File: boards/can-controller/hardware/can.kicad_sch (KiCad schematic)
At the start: 40 parts, among them J10 CAN1, J11 CAN2, J12 CAN3, J13 CAN4, U10 ISO1044BD, U11 ISO1044BD, U12 ISO1044BD, U13 ISO1044BD

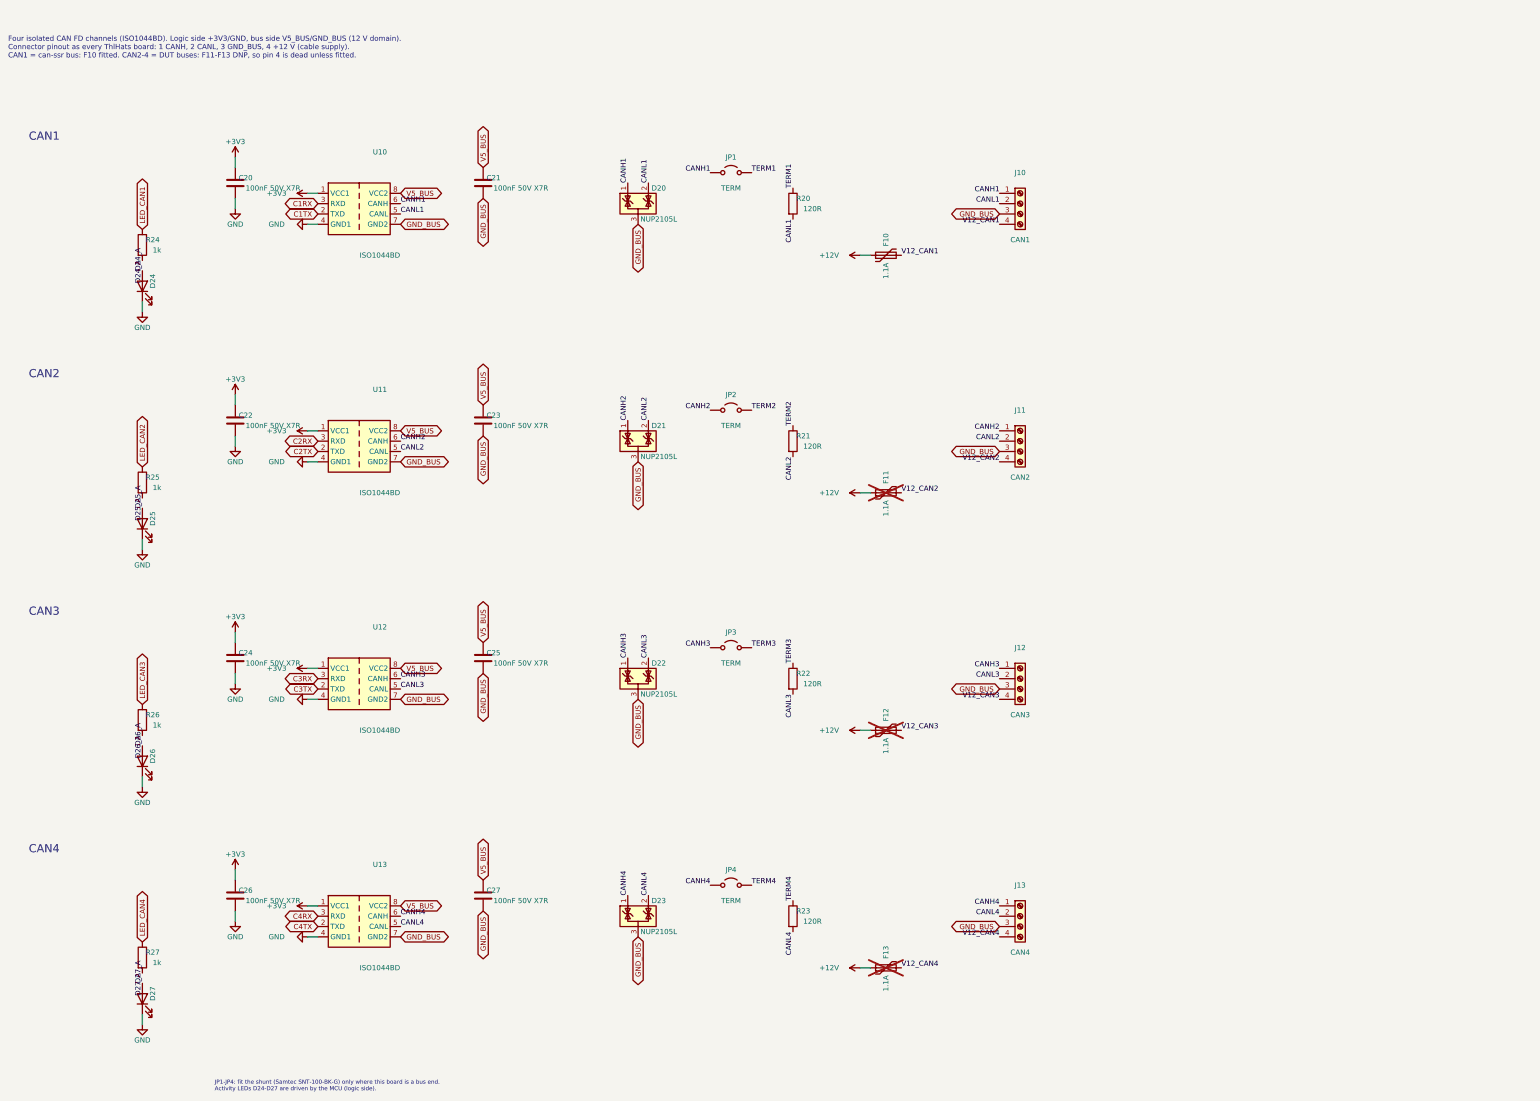
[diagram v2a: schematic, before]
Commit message: can-controller: schematic for the new scope (Ethernet W6100, 4 x ISOW1044, AQW212 relays, diff AI)
Six sheets generated by gen_schematic.py: MCU and logic power, Ethernet,
CAN x4, 12 V input and isolated logic supply (TDN 5-2411WI), relay drive,
GPIO and analog in. ERC 0; netlist check: no net crosses a domain except
at the designed crossings. New lib parts: Thl_Interface:W6100-L (flat),
Thl_Isolator:AQW212, stock ISOW1044 / TDN 5WI / LQFP-48 / bead footprints.
PCB still holds the old layout (next: update from schematic, placement).

Co-Authored-By: Claude Opus 5.5 <noreply@anthropic.com>
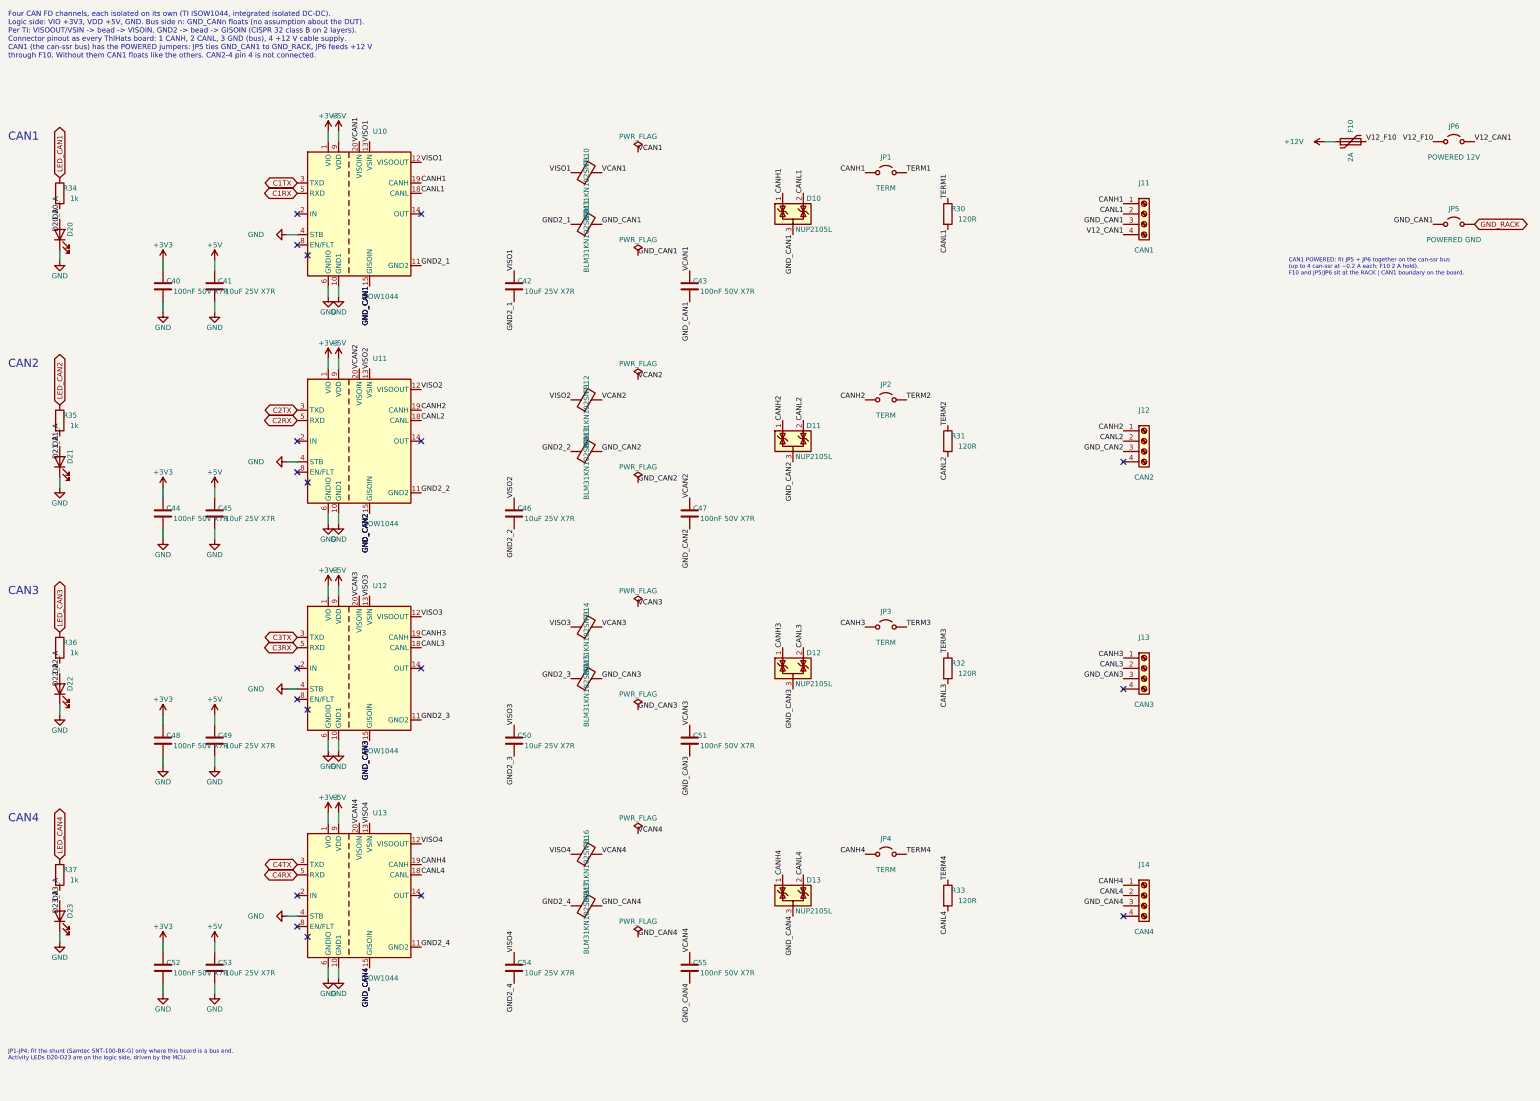
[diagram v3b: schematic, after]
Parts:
- removed C20, C21, C22, C23, C24, C25, C26, C27: 100nF 50V X7R, Capacitor_SMD:C_0805_2012Metric_Pad1.18x1.45mm_HandSolder, symbol Device:C
- removed D20, D21, D22, D23: NUP2105L, Package_TO_SOT_SMD:SOT-23, symbol Power_Protection:NUP2105L
- removed D24, D25, D26, D27: LED yellow, LED_SMD:LED_1206_3216Metric_Pad1.42x1.75mm_HandSolder, symbol Device:LED
- removed F11, F12, F13: 1.1A, Fuse:Fuse_1812_4532Metric_Pad1.30x3.40mm_HandSolder, symbol Device:Polyfuse
- removed J10: CAN1, Connector_Phoenix_MC:PhoenixContact_MC_1,5_4-G-3.5_1x04_P3.50mm_Horizontal, symbol Connector:Screw_Terminal_01x04
- removed R20, R21, R22, R23: 120R, Resistor_SMD:R_1206_3216Metric_Pad1.30x1.75mm_HandSolder, symbol Device:R
- removed R24, R25, R26, R27: 1k, Resistor_SMD:R_1206_3216Metric_Pad1.30x1.75mm_HandSolder, symbol Device:R
- removed U10, U11, U12, U13: ISO1044BD, Package_SO:SOIC-8_3.9x4.9mm_P1.27mm, symbol Interface_CAN_LIN:ISO1044BD
- added C40, C43, C44, C47, C48, C51, C52, C55: 100nF 50V X7R, Capacitor_SMD:C_0805_2012Metric_Pad1.18x1.45mm_HandSolder, symbol Device:C
- added C41, C42, C45, C46, C49, C50, C53, C54: 10uF 25V X7R, Capacitor_SMD:C_1206_3216Metric_Pad1.33x1.80mm_HandSolder, symbol Device:C
- added D10, D11, D12, D13: NUP2105L, Package_TO_SOT_SMD:SOT-23, symbol Power_Protection:NUP2105L
- added D20, D21, D22, D23: LED yellow, LED_SMD:LED_1206_3216Metric_Pad1.42x1.75mm_HandSolder, symbol Device:LED
- added FB10, FB11, FB12, FB13, FB14, FB15, FB16, FB17: BLM31KN102SN1L, Inductor_SMD:L_1206_3216Metric_Pad1.22x1.90mm_HandSolder, symbol Device:FerriteBead
- added J14: CAN4, Connector_Phoenix_MC:PhoenixContact_MC_1,5_4-G-3.5_1x04_P3.50mm_Horizontal, symbol Connector:Screw_Terminal_01x04
- added JP5: POWERED GND, Connector_PinHeader_2.54mm:PinHeader_1x02_P2.54mm_Vertical, symbol Jumper:Jumper_2_Open
- added JP6: POWERED 12V, Connector_PinHeader_2.54mm:PinHeader_1x02_P2.54mm_Vertical, symbol Jumper:Jumper_2_Open
- added R30, R31, R32, R33: 120R, Resistor_SMD:R_1206_3216Metric_Pad1.30x1.75mm_HandSolder, symbol Device:R
- added R34, R35, R36, R37: 1k, Resistor_SMD:R_1206_3216Metric_Pad1.30x1.75mm_HandSolder, symbol Device:R
- added U10, U11, U12, U13: ISOW1044, Package_SO:SOIC-20W_7.5x12.8mm_P1.27mm, symbol Interface_CAN_LIN:ISOW1044
- F10: value 1.1A -> 2A; MPN 1812L110/16DR -> MF-MSMF200/16X-2; Manufacturer Littelfuse -> Bourns
- J11: value CAN2 -> CAN1
- J12: value CAN3 -> CAN2
- J13: value CAN4 -> CAN3
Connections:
- net V12_CAN2 is gone; now on net V12_CAN1: J11.4 (Pin_4)
- net +3V3: now also C40.1, C44.1, C48.1, C52.1, U10.1 (VIO), U11.1 (VIO), U12.1 (VIO), U13.1 (VIO)
- net C1RX: now also U10.5 (RXD)
- net C1TX: now also U10.3 (TXD)
- net C2RX: now also U11.5 (RXD)
- net C2TX: now also U11.3 (TXD)
- net C3RX: now also U12.5 (RXD)
- net C3TX: now also U12.3 (TXD)
- net C4RX: now also U13.5 (RXD)
- net C4TX: now also U13.3 (TXD)
- net CANH1: now also J11.1 (Pin_1), D10.1 (K), U10.19 (CANH)
- net CANH2: now also J12.1 (Pin_1), D11.1 (K), U11.19 (CANH); no longer J11.1 (Pin_1)
- net CANH3: now also J13.1 (Pin_1), D12.1 (K), U12.19 (CANH); no longer J12.1 (Pin_1)
- net CANH4: now also D13.1 (K), J14.1 (Pin_1), U13.19 (CANH); no longer J13.1 (Pin_1)
- net CANL1: now also J11.2 (Pin_2), D10.2 (K), R30.2, U10.18 (CANL)
- net CANL2: now also J12.2 (Pin_2), D11.2 (K), R31.2, U11.18 (CANL); no longer J11.2 (Pin_2)
- net CANL3: now also J13.2 (Pin_2), D12.2 (K), R32.2, U12.18 (CANL); no longer J12.2 (Pin_2)
- net CANL4: now also D13.2 (K), J14.2 (Pin_2), R33.2, U13.18 (CANL); no longer J13.2 (Pin_2)
- net GND: now also C40.2, C41.2, C44.2, C45.2, C48.2, C49.2, C52.2, C53.2, D20.1 (K), D21.1 (K), D22.1 (K), D23.1 (K), U10.10 (GND1), U10.4 (STB), U10.6 (GNDIO), U11.10 (GND1), U11.4 (STB), U11.6 (GNDIO), U12.10 (GND1), U12.4 (STB), U12.6 (GNDIO), U13.10 (GND1), U13.4 (STB), U13.6 (GNDIO)
- net LED_CAN1: now also R34.1
- net LED_CAN2: now also R35.1
- net LED_CAN3: now also R36.1
- net LED_CAN4: now also R37.1
- net TERM1: now also R30.1
- net TERM2: now also R31.1
- net TERM3: now also R32.1
- net TERM4: now also R33.1
- net V12_CAN1: now also JP6.2 (B); no longer F10.2
- removed net GND_BUS: J11.3 (Pin_3), J12.3 (Pin_3), J13.3 (Pin_3)
- net V12_CAN3: no longer names the net of J12.4 (Pin_4)
- net V12_CAN4: no longer names the net of J13.4 (Pin_4)
- new net +5V: C41.1, C45.1, C49.1, C53.1, U10.9 (VDD), U11.9 (VDD), U12.9 (VDD), U13.9 (VDD)
- new net D20_A: D20.2 (A), R34.2
- new net D21_A: D21.2 (A), R35.2
- new net D22_A: D22.2 (A), R36.2
- new net D23_A: D23.2 (A), R37.2
- new net GND2_1: C42.2, FB11.1, U10.11 (GND2)
- new net GND2_2: C46.2, FB13.1, U11.11 (GND2)
- new net GND2_3: C50.2, FB15.1, U12.11 (GND2)
- new net GND2_4: C54.2, FB17.1, U13.11 (GND2)
- new net GND_CAN1: C43.2, D10.3 (A), FB11.2, J11.3 (Pin_3), JP5.1 (A), U10.15 (GISOIN), U10.16 (GISOIN), U10.17 (GISOIN)
- new net GND_CAN2: C47.2, D11.3 (A), FB13.2, J12.3 (Pin_3), U11.15 (GISOIN), U11.16 (GISOIN), U11.17 (GISOIN)
- new net GND_CAN3: C51.2, D12.3 (A), FB15.2, J13.3 (Pin_3), U12.15 (GISOIN), U12.16 (GISOIN), U12.17 (GISOIN)
- new net GND_CAN4: C55.2, D13.3 (A), FB17.2, J14.3 (Pin_3), U13.15 (GISOIN), U13.16 (GISOIN), U13.17 (GISOIN)
- new net GND_RACK: JP5.2 (B)
- new net V12_F10: F10.2, JP6.1 (A)
- new net VCAN1: C43.1, FB10.2, U10.20 (VISOIN)
- new net VCAN2: C47.1, FB12.2, U11.20 (VISOIN)
- new net VCAN3: C51.1, FB14.2, U12.20 (VISOIN)
- new net VCAN4: C55.1, FB16.2, U13.20 (VISOIN)
- new net VISO1: C42.1, FB10.1, U10.12 (VISOOUT), U10.13 (VSIN)
- new net VISO2: C46.1, FB12.1, U11.12 (VISOOUT), U11.13 (VSIN)
- new net VISO3: C50.1, FB14.1, U12.12 (VISOOUT), U12.13 (VSIN)
- new net VISO4: C54.1, FB16.1, U13.12 (VISOOUT), U13.13 (VSIN)
- no-connect marks 0 -> 19
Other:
- note added: "CAN1 POWERED: fit JP5 + JP6 together on the can-ssr bus (up to 4 can-ssr at ~0.2 A each; F10 2 A hold). F10 and JP5/JP6 sit at the RACK | CAN1 boundary on the board."
- note added: "Four CAN FD channels, each isolated on its own (TI ISOW1044, integrated isolated DC-DC). Logic side: VIO +3V3, VDD +5V, GND. Bus side n: GND_CANn floats (no assumption about the DUT). Per TI: VISOOUT/VSIN -> bead -> VISOIN, GND2 -> bead -> GISOIN (CISPR 32 class B on 2 layers). Connector pinout as every ThlHats board: 1 CANH, 2 CANL, 3 GND (bus), 4 +12 V cable supply. CAN1 (the can-ssr bus) has t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"
- note added: "JP1-JP4: fit the shunt (Samtec SNT-100-BK-G) only where this board is a bus end. Activity LEDs D20-D23 are on the logic side, driven by the MCU."
- note removed: "Four isolated CAN FD channels (ISO1044BD). Logic side +3V3/GND, bus side V5_BUS/GND_BUS (12 V domain). Connector pinout as every ThlHats board: 1 CANH, 2 CANL, 3 GND_BUS, 4 +12 V (cable supply). CAN1 = can-ssr bus: F10 fitted. CAN2-4 = DUT buses: F11-F13 DNP, so pin 4 is dead unless fitted."
- note removed: "JP1-JP4: fit the shunt (Samtec SNT-100-BK-G) only where this board is a bus end. Activity LEDs D24-D27 are driven by the MCU (logic side)."
